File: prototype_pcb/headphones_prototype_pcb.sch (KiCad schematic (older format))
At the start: 51 parts, among them J1 LIGHTING_JACK, J2 CONN_01X10, J3 BOTTOM_FLEX_LIGHTNING, J4 CONN_01X10, J5 LIGHTNING_HEADPHONE_ADAPTER, J6 CONN_01X10, J7 IPHONE_HEADPHONE_JACK, J8 CONN_01X02, U1 SN74LVC1G123, U2 ADG774A, U3 SN74LVC1G123, U4 NC7S32

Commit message: Rigid prototype pcb v1.2
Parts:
- added J10: CONN_01X05, Pin_Headers:Pin_Header_Straight_1x05_Pitch2.54mm, symbol CONN_01X05
- added J9: LIGHTNING_HEADPHONE_ADAPTER, lightning_headphone_adapter:LIGHTNING_HEADPHONE_ADAPTER_HANDWIRE, symbol LIGHTNING_HEADPHONE_ADAPTER
- J5: footprint lightning_headphone_adapter:LIGHTNING_HEADPHONE_ADAPTER -> lightning_headphone_adapter:LIGHTNING_HEADPHONE_ADAPTER_CASTELLATED
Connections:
- net GNDREF: now also J9.2 (PIN_1)
- net HPIN2: now also J9.3 (PIN_2)
- net HPIN3: now also J9.4 (PIN_3)
- net HPIN4: now also J9.5 (PIN_4)
- net at J5.1 (L_SHIELD), J6.1 (P1): now also J9.1 (L_SHIELD)
- net at J5.6 (PIN_5), J6.6 (P6), JP31.1: now also J9.6 (PIN_5)
- net at J5.7 (PIN_6), J6.7 (P7), JP32.1: now also J9.7 (PIN_6)
- net at J5.8 (PIN_7), J6.8 (P8), JP33.1: now also J9.8 (PIN_7)
- net at J5.9 (PIN_8), J6.9 (P9), JP34.1: now also J9.9 (PIN_8)
- net at J5.14 (Si), J5.17 (S), J7.1 (S): now also J10.1 (P1), J9.14 (Si), J9.17 (S)
- net at J5.11 (R1), J7.2 (R1): now also J10.2 (P2), J9.11 (R1)
- net at J5.15 (T2), J7.3 (T2): now also J10.3 (P3), J9.15 (T2)
- net at J5.13 (T1), J7.4 (T1): now also J10.4 (P4), J9.13 (T1)
- net at J5.12 (R2i), J5.16 (R2), J7.5 (R2): now also J10.5 (P5), J9.12 (R2i), J9.16 (R2)
- no-connect marks 0 -> 2
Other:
- moved on the sheet: C1, C2, J1, J2, J3, J4, J5, J6, J7, J8, R1, R2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

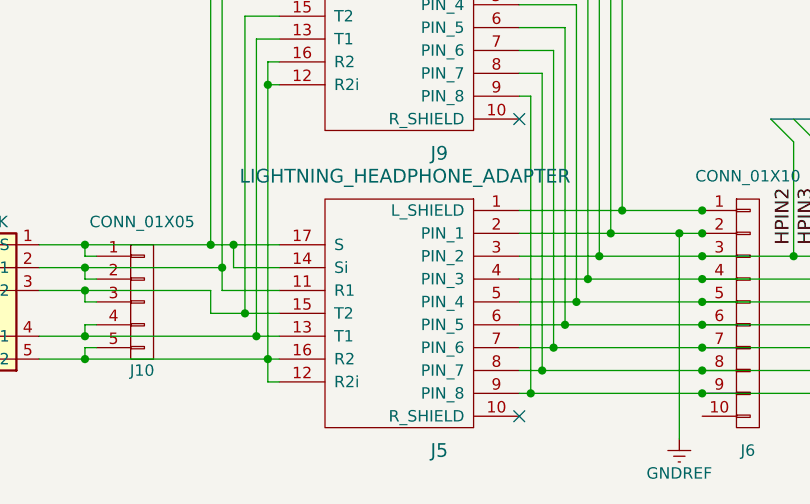
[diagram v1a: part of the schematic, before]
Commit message: Remove castellated edges adapter from prototype
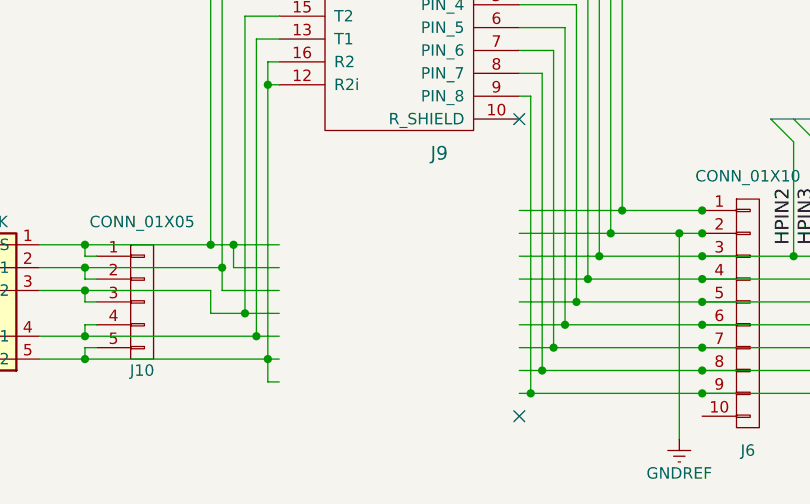
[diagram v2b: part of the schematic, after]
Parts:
- removed J5: LIGHTNING_HEADPHONE_ADAPTER, lightning_headphone_adapter:LIGHTNING_HEADPHONE_ADAPTER_CASTELLATED, symbol LIGHTNING_HEADPHONE_ADAPTER
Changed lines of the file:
@@
 Wire Wire Line
 	7150 2350 7150 2400
-$Comp
-L LIGHTNING_HEADPHONE_ADAPTER J5
-U 1 1 59267C0B
-P 3400 5400
-F 0 "J5" H 3400 4600 60  0000 C CNN
-F 1 "LIGHTNING_HEADPHONE_ADAPTER" H 3550 5800 60  0000 C CNN
-F 2 "lightning_headphone_adapter:LIGHTNING_HEADPHONE_ADAPTER_CASTELLATED" H 3400 5400 60  0001 C CNN
-F 3 "" H 3400 5400 60  0001 C CNN
-	1    3400 5400
-	-1   0    0    -1
-$EndComp
 Wire Wire Line
 	1650 5300 2700 5300
